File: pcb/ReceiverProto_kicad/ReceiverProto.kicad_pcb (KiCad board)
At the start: 2 copper layers, 60 parts, among them J1 Conn_01x09, J2 Conn_01x02, J3 Conn_01x04, J4 Conn_01x06, U11 ADM8660ARZ-REEL, U12 ADP7182AUJZ-1.8-R7, U13 ADA4807-1, U14 ADA4807-1, U15 ADA4807-1, U16 ADA4807-1, U4 AD7387BCPZ-RL7, U5 TLV9001IDCK, U6 TLV9001IDCK

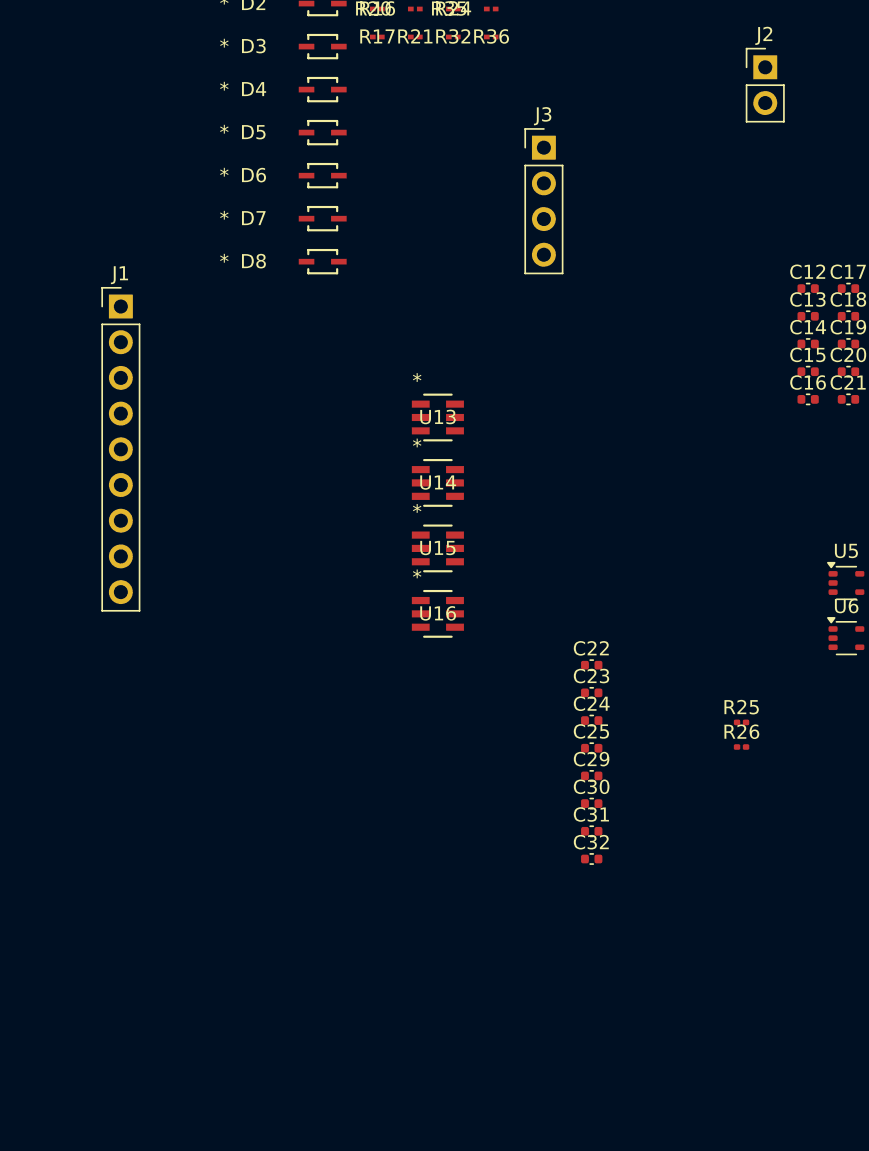
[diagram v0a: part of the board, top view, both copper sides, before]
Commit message: fixed kicad project, all footprints linked and no errors on board
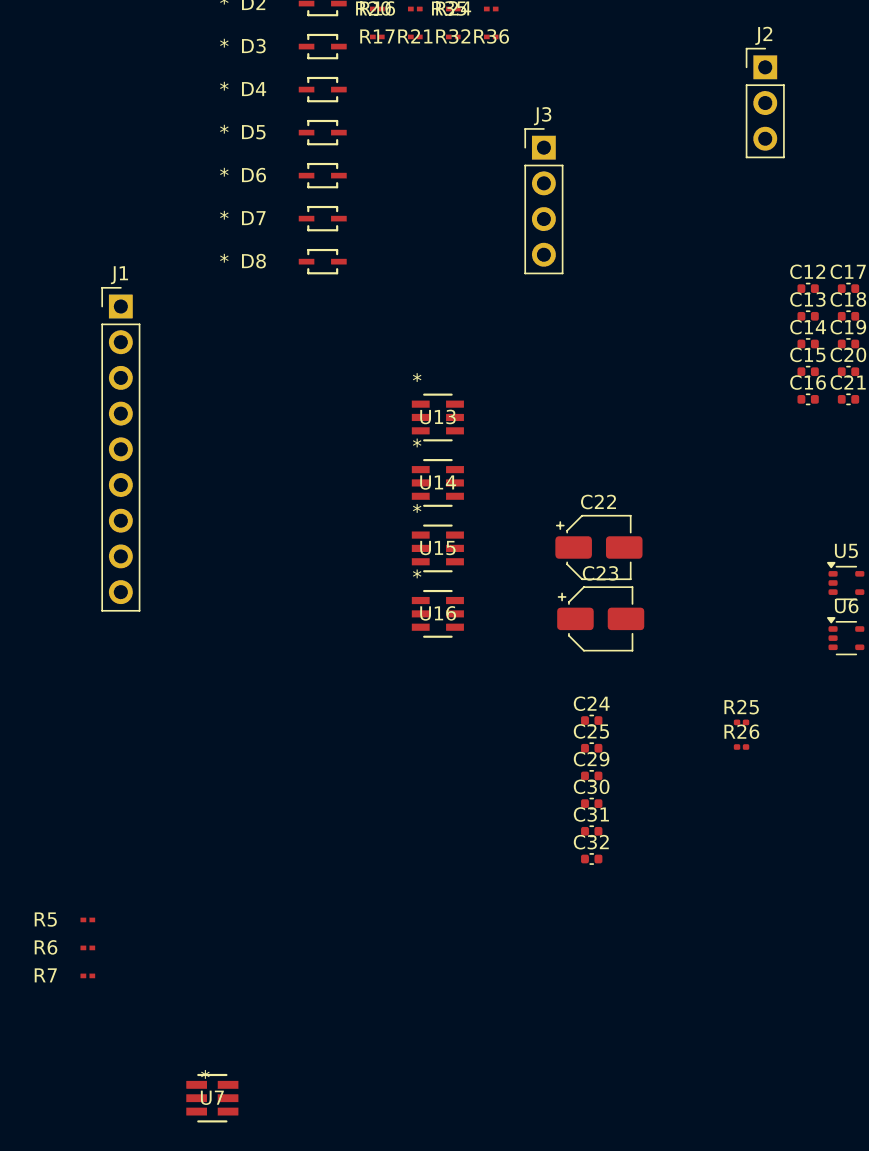
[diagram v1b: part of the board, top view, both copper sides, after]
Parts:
- added R5: 100, SMD_Passives:YAG_R0201_YAG_100, F.Cu at (91.9, 105.2)
- added R6: 100, SMD_Passives:YAG_R0201_YAG_100, F.Cu at (91.9, 107.2)
- added R7: 100, SMD_Passives:YAG_R0201_YAG_100, F.Cu at (91.9, 109.2)
- added U7: TPS79301DBVR, Voltage_Regulator:DBV6, F.Cu at (100.7, 117.9)
- C22, C23: footprint Capacitor_SMD:C_0402_1005Metric -> Capacitor_SMD:CP_Elec_4x5.8
- J2: value Conn_01x02 -> Conn_01x03; footprint Connector_PinHeader_2.54mm:PinHeader_1x02_P2.54mm_Vertical -> Connector_PinHeader_2.54mm:PinHeader_1x03_P2.54mm_Vertical
- moved C22 8.39 mm to (128.2, 78.7)
- moved C23 5.30 mm to (128.4, 83.8)
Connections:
- J2 pad 2: 0 -> +3V3
- J4 pad 1: ADC_SDI -> Net-(J4-Pin_1)
- J4 pad 4: ADC_SCLK -> Net-(J4-Pin_4)
- J4 pad 5: ADC_CS -> Net-(J4-Pin_5)

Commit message: inital pcb layout edits, placed components roughly where the need to be.
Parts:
- moved R13 100.1 mm to (153.2, 127.9)
- moved R14 100.1 mm to (153.2, 129.9)
- moved R16 100.1 mm to (153.2, 131.9)
- moved R17 100.1 mm to (153.2, 133.9)
- moved R18 100.1 mm to (155.9, 127.9)
- moved R19 100.1 mm to (155.9, 129.9)
- moved R20 100.1 mm to (155.9, 131.9)
- moved R21 100.1 mm to (155.9, 133.9)
- moved R22 100.1 mm to (158.6, 127.9)
- moved R23 100.1 mm to (158.6, 129.9)
- moved R24 100.1 mm to (158.6, 131.9)
- moved R32 100.1 mm to (158.6, 133.9)
- moved R33 100.1 mm to (161.3, 127.9)
- moved R34 100.1 mm to (161.3, 129.9)
- moved R35 100.1 mm to (161.3, 131.9)
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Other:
- board outline added: 75 x 50 mm

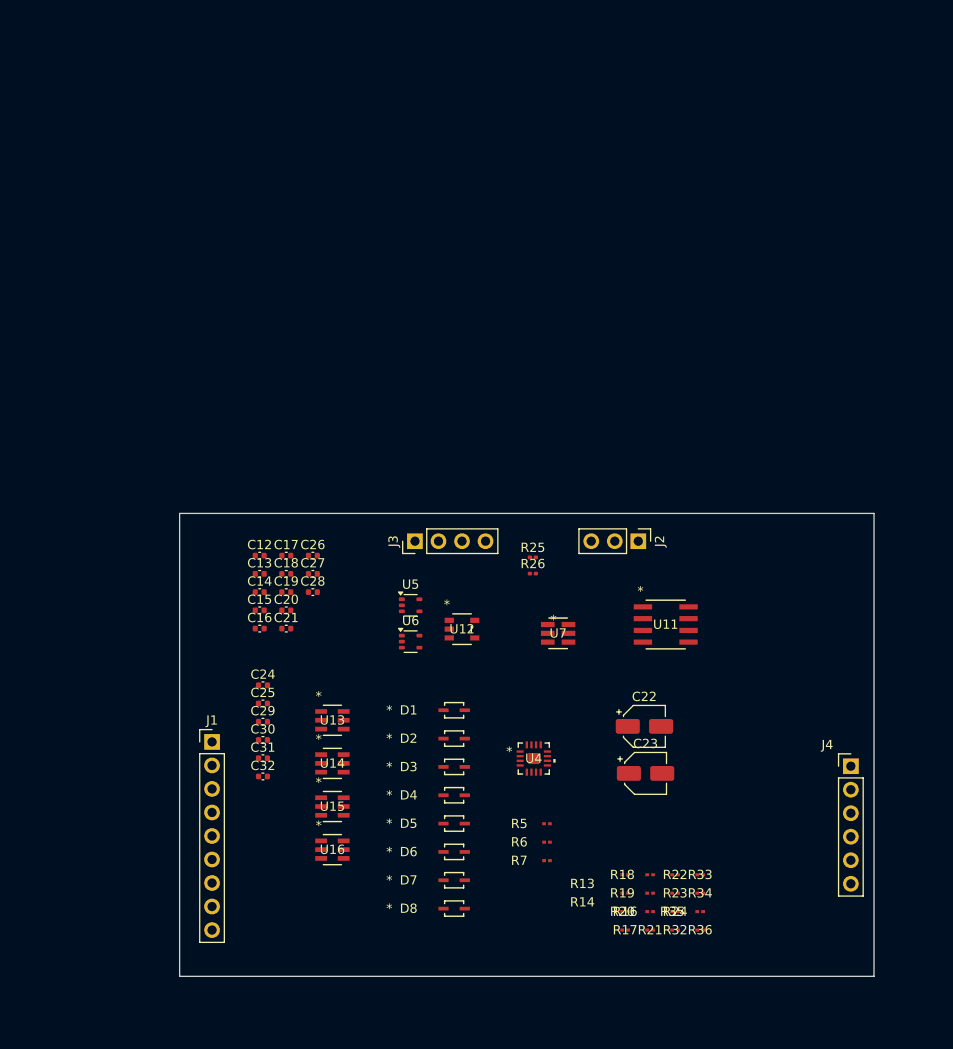
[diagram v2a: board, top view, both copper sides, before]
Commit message: added design rules, ground plane
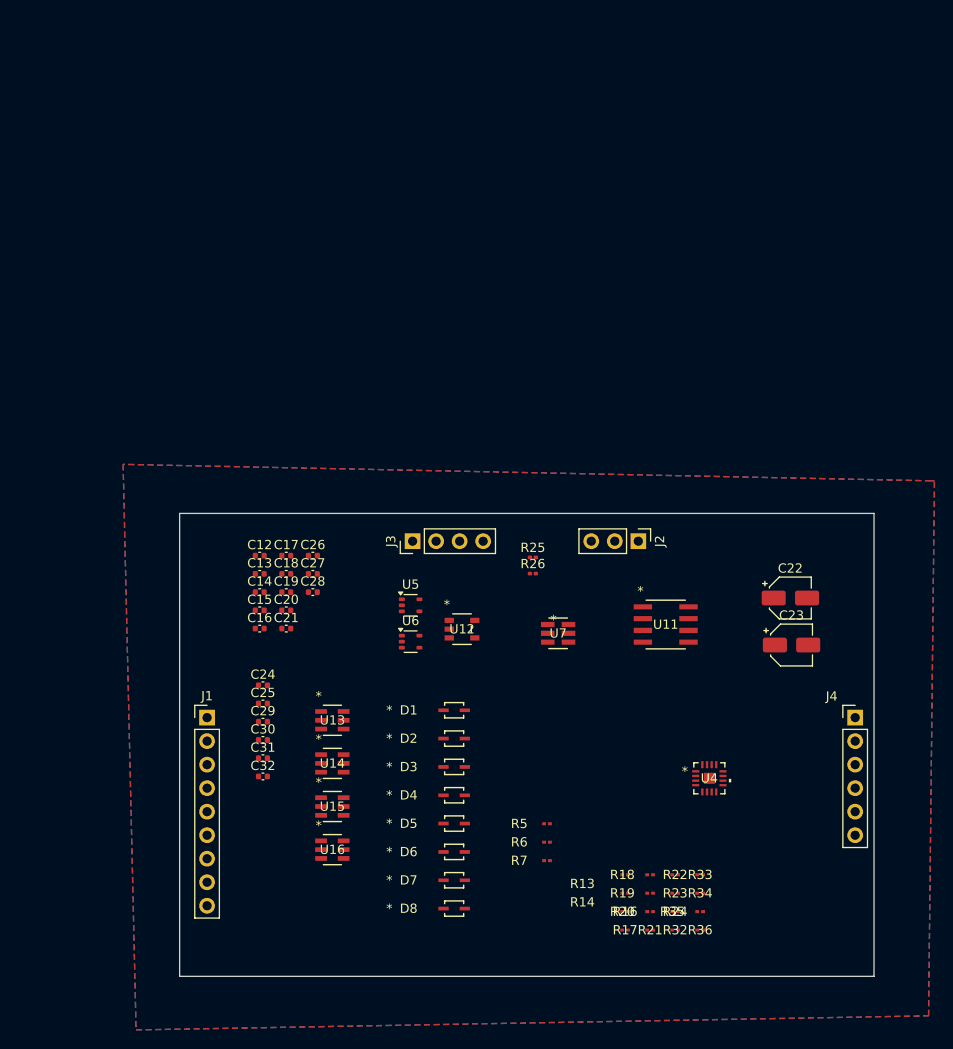
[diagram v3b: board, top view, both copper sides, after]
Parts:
- moved C22 21.0 mm to (171.0, 98.0)
- moved C23 21.0 mm to (171.1, 103.1)
- moved U4 19.1 mm to (162.2, 117.5)
- moved J4 5.27 mm to (178.0, 110.9)
- moved J1 2.68 mm to (108.0, 110.9)
- moved J3 0.26 mm to (130.2, 91.9)
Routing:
- added copper zone on B.Cu, net 0
- added copper zone on F.Cu, net 0
- added copper zone on In1.Cu, net 0
- added copper zone on In2.Cu, net 0
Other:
- copper layers 2 -> 4
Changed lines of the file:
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@@
 	(layers
 		(0 "F.Cu" signal)
+		(4 "In1.Cu" signal)
+		(6 "In2.Cu" signal)
 		(2 "B.Cu" signal)
 		(9 "F.Adhes" user "F.Adhesive")
@@
 	)
 	(setup
+		(stackup
+			(layer "F.SilkS"
+				(type "Top Silk Screen")
+			)
+			(layer "F.Paste"
+				(type "Top Solder Paste")
+			)
+			(layer "F.Mask"
+				(type "Top Solder Mask")
+				(thickness 0.01)
+			)
+			(layer "F.Cu"
+				(type "copper")
+				(thickness 0.035)
+			)
+			(layer "dielectric 1"
+				(type "prepreg")
+				(thickness 0.1)
+				(material "FR4")
+				(epsilon_r 4.5)
+				(loss_tangent 0.02)
+			)
+			(layer "In1.Cu"
+				(type "copper")
+				(thickness 0.035)
+			)
+			(layer "dielectric 2"
+				(type "core")
+				(thickness 1.24)
+				(material "FR4")
+				(epsilon_r 4.5)
+				(loss_tangent 0.02)
+			)
+			(layer "In2.Cu"
+				(type "copper")
+				(thickness 0.035)
+			)
+			(layer "dielectric 3"
+				(type "prepreg")
+				(thickness 0.1)
+				(material "FR4")
+				(epsilon_r 4.5)
+				(loss_tangent 0.02)
+			)
+			(layer "B.Cu"
+				(type "copper")
+				(thickness 0.035)
+			)
+			(layer "B.Mask"
+				(type "Bottom Solder Mask")
+				(thickness 0.01)
+			)
+			(layer "B.Paste"
+				(type "Bottom Solder Paste")
+			)
+			(layer "B.SilkS"
+				(type "Bottom Silk Screen")
+			)
+			(copper_finish "HAL lead-free")
+			(dielectric_constraints no)
+		)
 		(pad_to_mask_clearance 0)
 		(allow_soldermask_bridges_in_footprints no)
@@
 	(footprint "adc:CP-16-45_ADI"
 		(layer "F.Cu")
-		(at 143.286201 115.3382)
+		(at 162.249999 117.4732)
 		(tags "AD7387BCPZ-RL7 ")
 		(property "Reference" "U4"
@@
 	(footprint "Capacitor_SMD:CP_Elec_4x5.8"
 		(layer "F.Cu")
-		(at 155.3632 116.945)
+		(at 171.127 103.08)
 		(descr "SMD capacitor, aluminum electrolytic, Panasonic, 4.0x5.8mm")
 		(tags "capacitor electrolytic")
@@
 	(footprint "Capacitor_SMD:CP_Elec_4x5.8"
 		(layer "F.Cu")
-		(at 155.2362 111.865)
+		(at 171 98)
 		(descr "SMD capacitor, aluminum electrolytic, Panasonic, 4.0x5.8mm")
 		(tags "capacitor electrolytic")
@@
 	(footprint "Connector_PinHeader_2.54mm:PinHeader_1x04_P2.54mm_Vertical"
 		(layer "F.Cu")
-		(at 130.4562 91.865 90)
+		(at 130.2 91.865 90)
 		(descr "Through hole straight pin header, 1x04, 2.54mm pitch, single row")
 		(tags "Through hole pin header THT 1x04 2.54mm single row")
@@
 	(footprint "Connector_PinHeader_2.54mm:PinHeader_1x06_P2.54mm_Vertical"
 		(layer "F.Cu")
-		(at 177.5362 116.165)
+		(at 178 110.92)
 		(descr "Through hole straight pin header, 1x06, 2.54mm pitch, single row")
 		(tags "Through hole pin header THT 1x06 2.54mm single row")
@@
 	(footprint "Connector_PinHeader_2.54mm:PinHeader_1x09_P2.54mm_Vertical"
 		(layer "F.Cu")
-		(at 108.5362 113.545)
+		(at 108 110.92)
 		(descr "Through hole straight pin header, 1x09, 2.54mm pitch, single row")
 		(tags "Through hole pin header THT 1x09 2.54mm single row")
@@
 		(layer "Edge.Cuts")
 	)
+	(zone
+		(net 4)
+		(net_name "0")
+		(layers "F.Cu" "B.Cu" "In1.Cu" "In2.Cu")
+		(hatch edge 0.5)
+		(connect_pads
+			(clearance 0.5)
+		)
+		(min_thickness 0.25)
+		(filled_areas_thickness no)
+		(fill yes
+			(thermal_gap 0.5)
+			(thermal_bridge_width 0.5)
+		)
+		(polygon
+			(pts
+				(xy 186.182 85.344) (xy 98.933 83.566) (xy 100.33 144.653) (xy 185.928 143.129) (xy 186.563 85.344)
+			)
+		)
+	)
 	(embedded_fonts no)

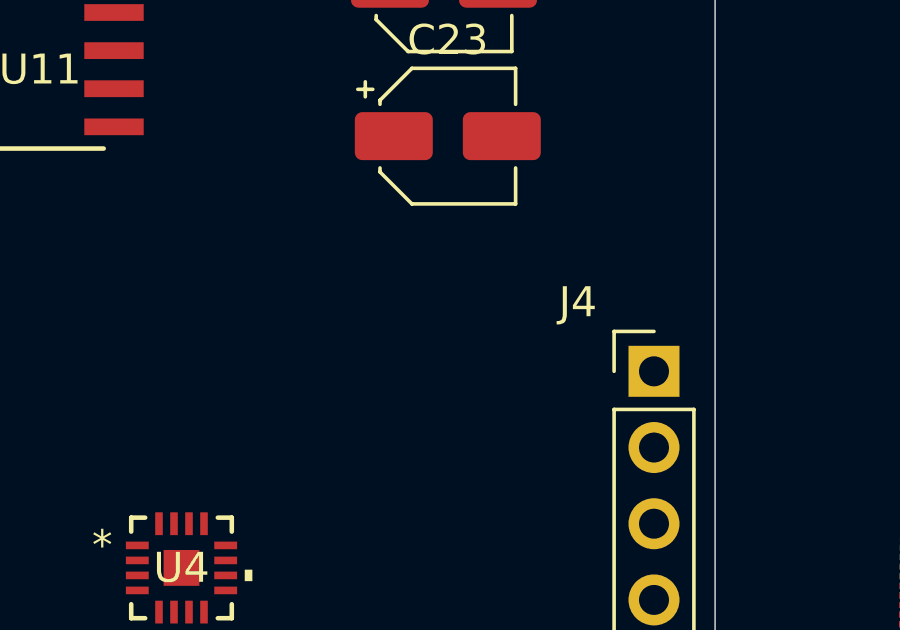
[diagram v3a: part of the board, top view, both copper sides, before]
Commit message: add 5V filtering cap, reordered analog input pins
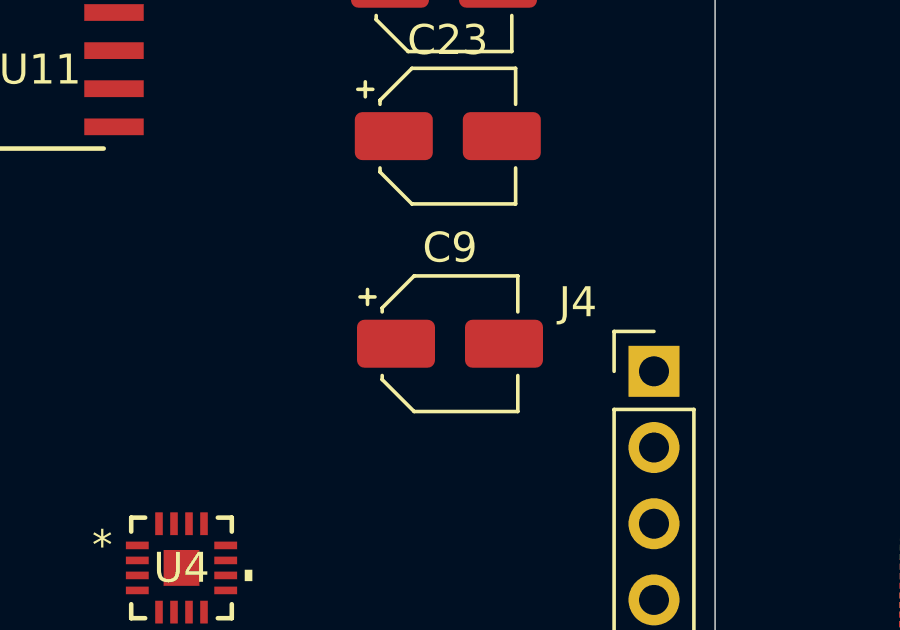
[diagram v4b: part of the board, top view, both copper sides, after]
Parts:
- added C9: 10u, Capacitor_SMD:CP_Elec_4x5.8, F.Cu at (171.2, 110.0)
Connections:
- J1 pad 2: ADC_A0 -> ADC_B1
- J1 pad 4: ADC_A1 -> ADC_B0
- J1 pad 6: ADC_B0 -> ADC_A1
- J1 pad 8: ADC_B1 -> ADC_A0

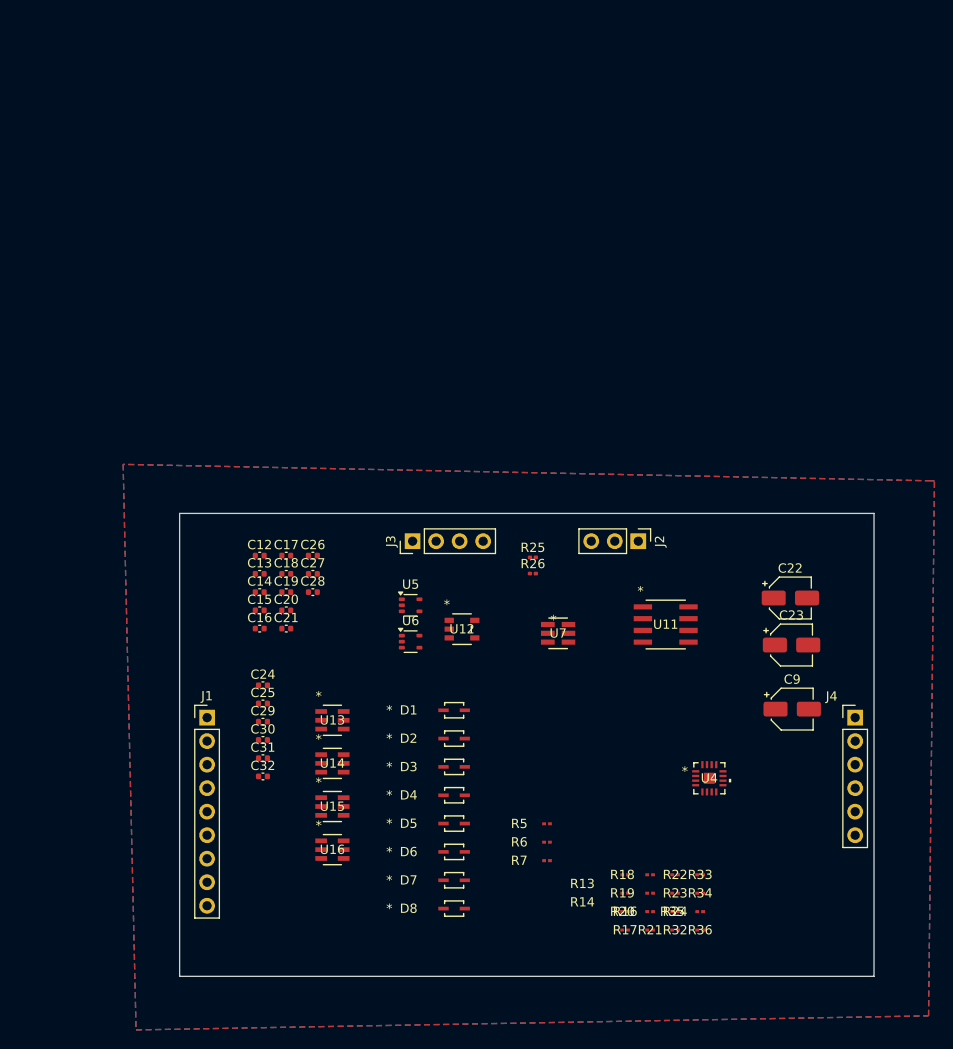
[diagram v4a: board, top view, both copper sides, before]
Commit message: major progress on board layout, slight schematic tweaks for ease of routing
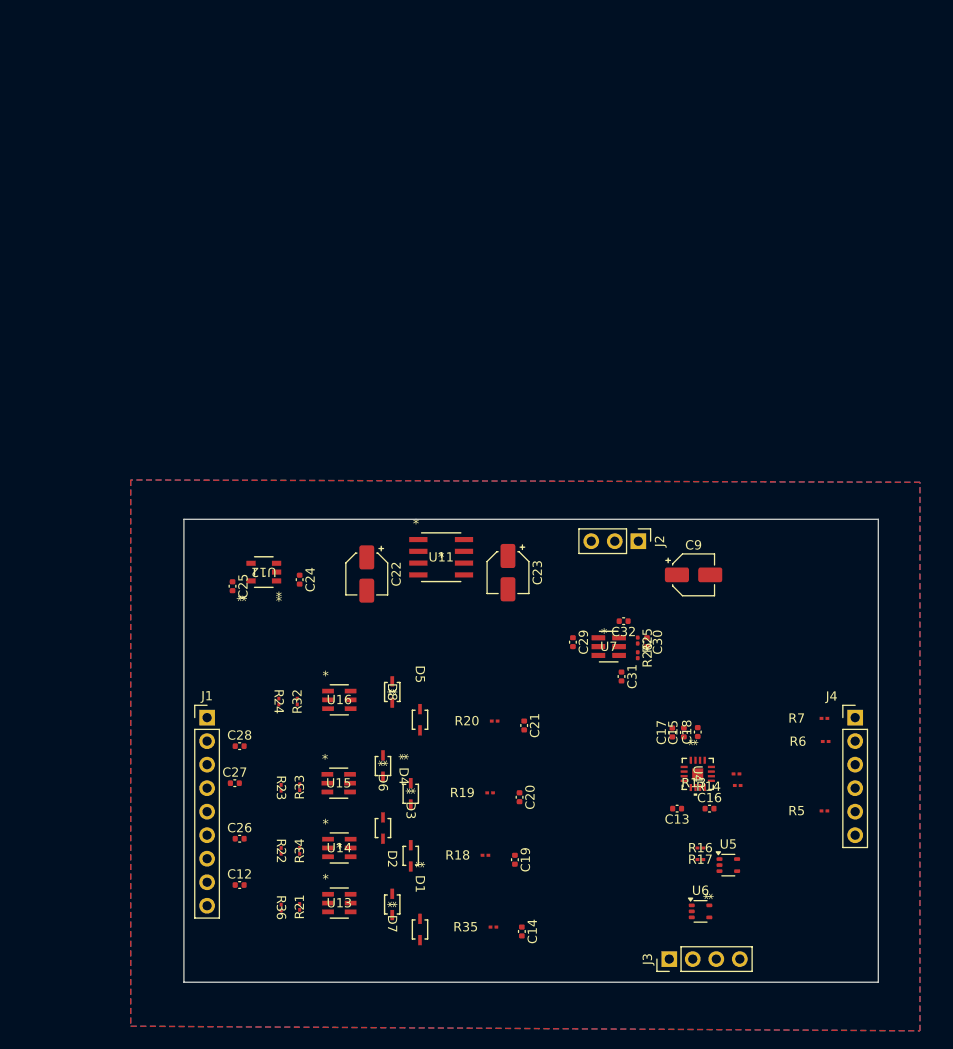
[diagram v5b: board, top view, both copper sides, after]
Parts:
- moved J3 53.0 mm to (157.9, 137.0)
- moved C16 52.3 mm to (162.3, 120.8)
- moved C13 51.7 mm to (158.8, 120.8), turned to 180 degrees
- moved R24 48.4 mm to (115.8, 109.2), turned to -90 degrees
- moved R32 47.7 mm to (117.8, 109.2), turned to 90 degrees
- moved C15 47.7 mm to (159.5, 112.5), turned to 90 degrees
- moved C18 47.6 mm to (161.0, 112.5), turned to 90 degrees
- moved C14 46.3 mm to (142.0, 134.0), turned to -90 degrees
- moved C17 45.9 mm to (158.2, 112.5), turned to 90 degrees
- moved C22 45.8 mm to (125.2, 95.4), turned to -90 degrees
- moved R36 45.3 mm to (116.0, 131.4), turned to -90 degrees
- moved U5 44.3 mm to (164.3, 126.8)
- moved R33 44.3 mm to (118.0, 118.4), turned to 90 degrees
- moved R23 44.1 mm to (116.0, 118.5), turned to -90 degrees
- moved R34 43.5 mm to (118.0, 125.3), turned to 90 degrees
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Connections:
- J4 pad 2: ADC_SDOA -> Net-(J4-Pin_2)
- J4 pad 4: Net-(J4-Pin_4) -> ADC_SDOA
- R6 pad 1: ADC_SCLK -> ADC_SDI
- R6 pad 2: Net-(J4-Pin_4) -> Net-(J4-Pin_2)
- R7 pad 1: ADC_SDI -> ADC_SCLK
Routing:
- added copper zone on In2.Cu, net +3V3
- added copper zone on In2.Cu, net +5V
- added copper zone on In2.Cu, net -2V5
- added copper zone on In2.Cu, net -5V
- removed copper zone on In2.Cu, net 0
